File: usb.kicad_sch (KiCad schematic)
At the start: 14 parts, among them J201 GT-USB-7010ASV, Q201 S8050, Q202 S8050, U202 CP2104

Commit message: Update to kicad 9
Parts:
- J201: value GT-USB-7010ASV -> GT-USB-7010ASV

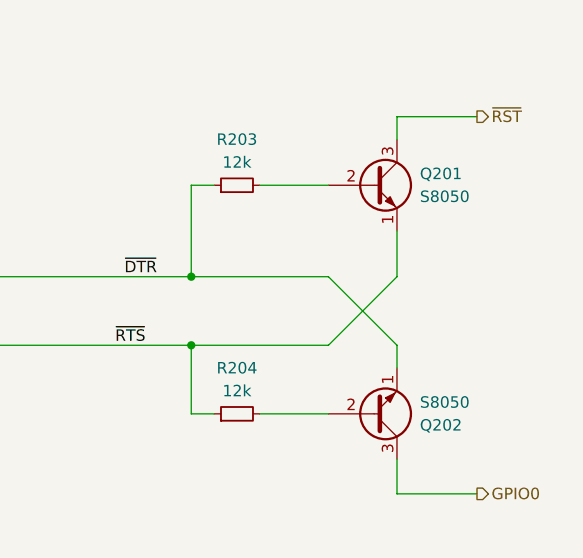
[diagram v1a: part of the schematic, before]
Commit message: Fix hardware flow control transistor pinouts
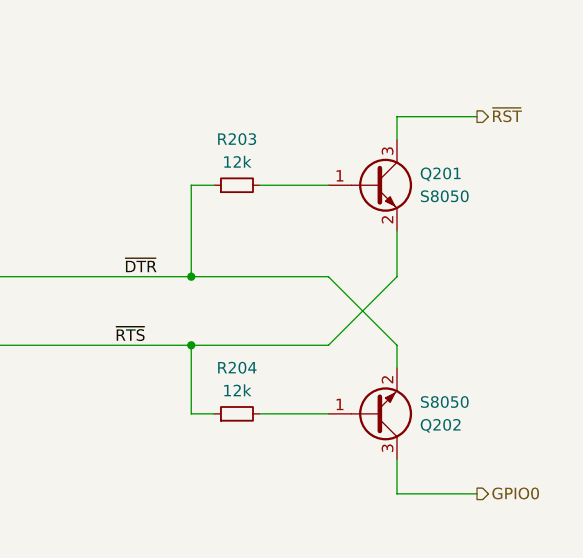
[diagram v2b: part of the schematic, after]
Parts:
- Q201, Q202: symbol Transistor_BJT:S8050 -> Transistor_BJT:Q_NPN_BEC
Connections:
- net ~{DTR}: now also Q202.2 (E); no longer Q202.1 (E)
- net ~{RTS}: now also Q201.2 (E); no longer Q201.1 (E)
- net at R204.2: now also Q202.1 (B); no longer Q202.2 (B)
- net at R203.2: now also Q201.1 (B); no longer Q201.2 (B)
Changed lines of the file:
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@@
 	)
 	(symbol
-		(lib_id "Transistor_BJT:S8050")
+		(lib_id "Transistor_BJT:Q_NPN_BEC")
 		(at 256.54 119.38 0)
 		(mirror x)
@@
 		)
 		(property "Footprint" "Package_TO_SOT_SMD:SOT-23-3"
-			(at 261.62 117.475 0)
-			(effects
-				(font
-					(size 1.27 1.27)
-					(italic yes)
-				)
-				(justify left)
-				(hide yes)
-			)
-		)
-		(property "Datasheet" "http://www.unisonic.com.tw/datasheet/S8050.pdf"
+			(at 261.62 121.92 0)
+			(effects
+				(font
+					(size 1.27 1.27)
+				)
+				(hide yes)
+			)
+		)
+		(property "Datasheet" "https://www.lcsc.com/datasheet/C2891804.pdf"
 			(at 256.54 119.38 0)
 			(effects
@@
 					(size 1.27 1.27)
 				)
-				(justify left)
-				(hide yes)
-			)
-		)
-		(property "Description" "0.7A Ic, 20V Vce, Low Voltage High Current NPN Transistor, TO-92"
+				(hide yes)
+			)
+		)
+		(property "Description" "Bipolar (BJT) Transistor NPN 25 V 500 mA 150MHz 300 mW Surface Mount SOT-23"
 			(at 256.54 119.38 0)
 			(effects
@@
 	)
 	(symbol
-		(lib_id "Transistor_BJT:S8050")
+		(lib_id "Transistor_BJT:Q_NPN_BEC")
 		(at 256.54 93.98 0)
 		(unit 1)
@@
 		(fields_autoplaced yes)
 		(property "Reference" "Q201"
-			(at 261.62 92.71 0)
+			(at 261.62 92.7099 0)
 			(effects
 				(font
@@
 		)
 		(property "Value" "S8050"
-			(at 261.62 95.25 0)
+			(at 261.62 95.2499 0)
 			(effects
 				(font
@@
 		)
 		(property "Footprint" "Package_TO_SOT_SMD:SOT-23-3"
-			(at 261.62 95.885 0)
-			(effects
-				(font
-					(size 1.27 1.27)
-					(italic yes)
-				)
-				(justify left)
-				(hide yes)
-			)
-		)
-		(property "Datasheet" "http://www.unisonic.com.tw/datasheet/S8050.pdf"
+			(at 261.62 91.44 0)
+			(effects
+				(font
+					(size 1.27 1.27)
+				)
+				(hide yes)
+			)
+		)
+		(property "Datasheet" "https://www.lcsc.com/datasheet/C2891804.pdf"
 			(at 256.54 93.98 0)
 			(effects
@@
 					(size 1.27 1.27)
 				)
-				(justify left)
-				(hide yes)
-			)
-		)
-		(property "Description" "0.7A Ic, 20V Vce, Low Voltage High Current NPN Transistor, TO-92"
+				(hide yes)
+			)
+		)
+		(property "Description" "Bipolar (BJT) Transistor NPN 25 V 500 mA 150MHz 300 mW Surface Mount SOT-23"
 			(at 256.54 93.98 0)
 			(effects

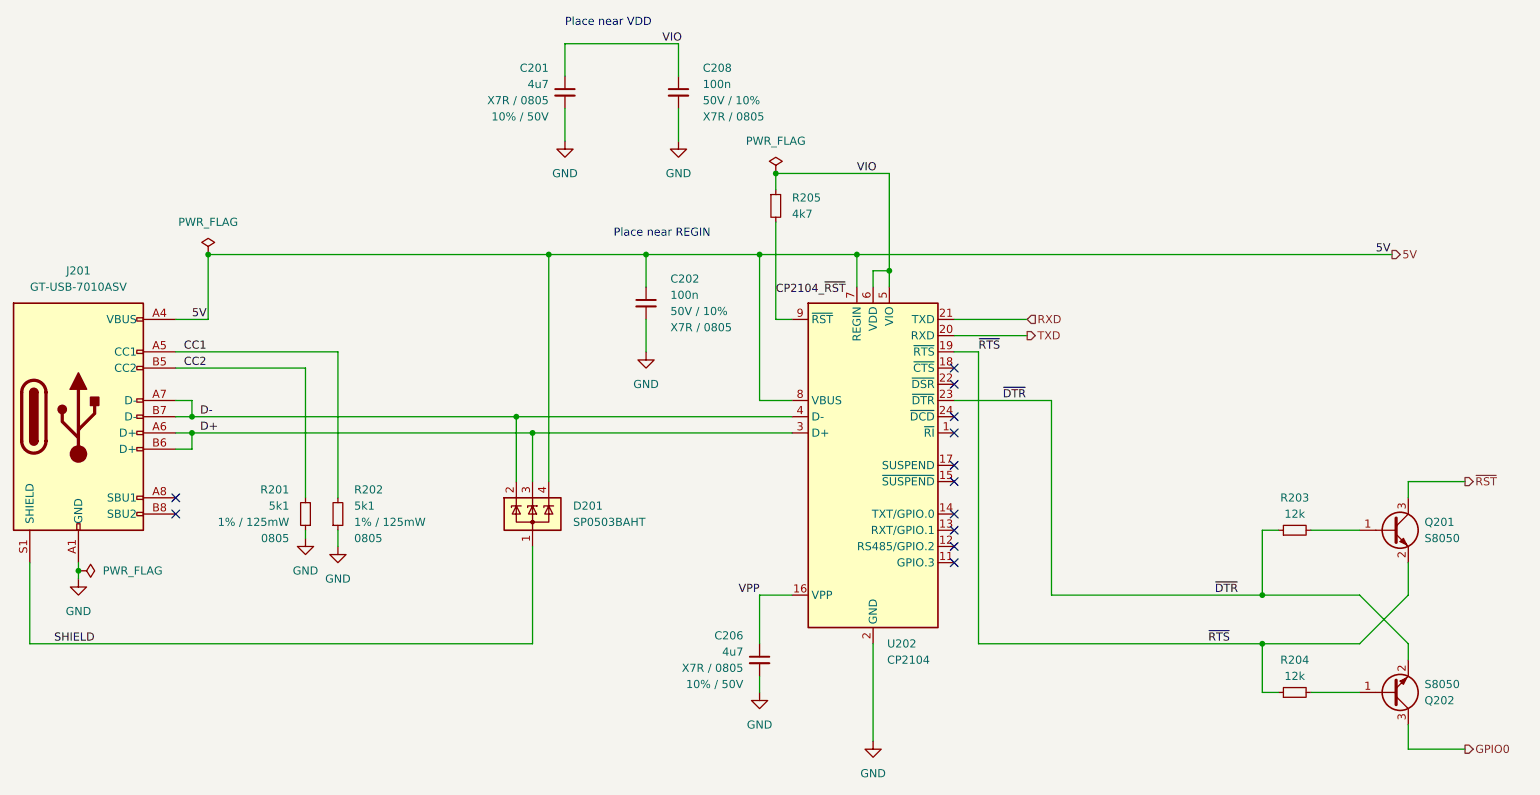
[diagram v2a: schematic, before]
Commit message: Update reference designators to single digit
Fits on the silk better
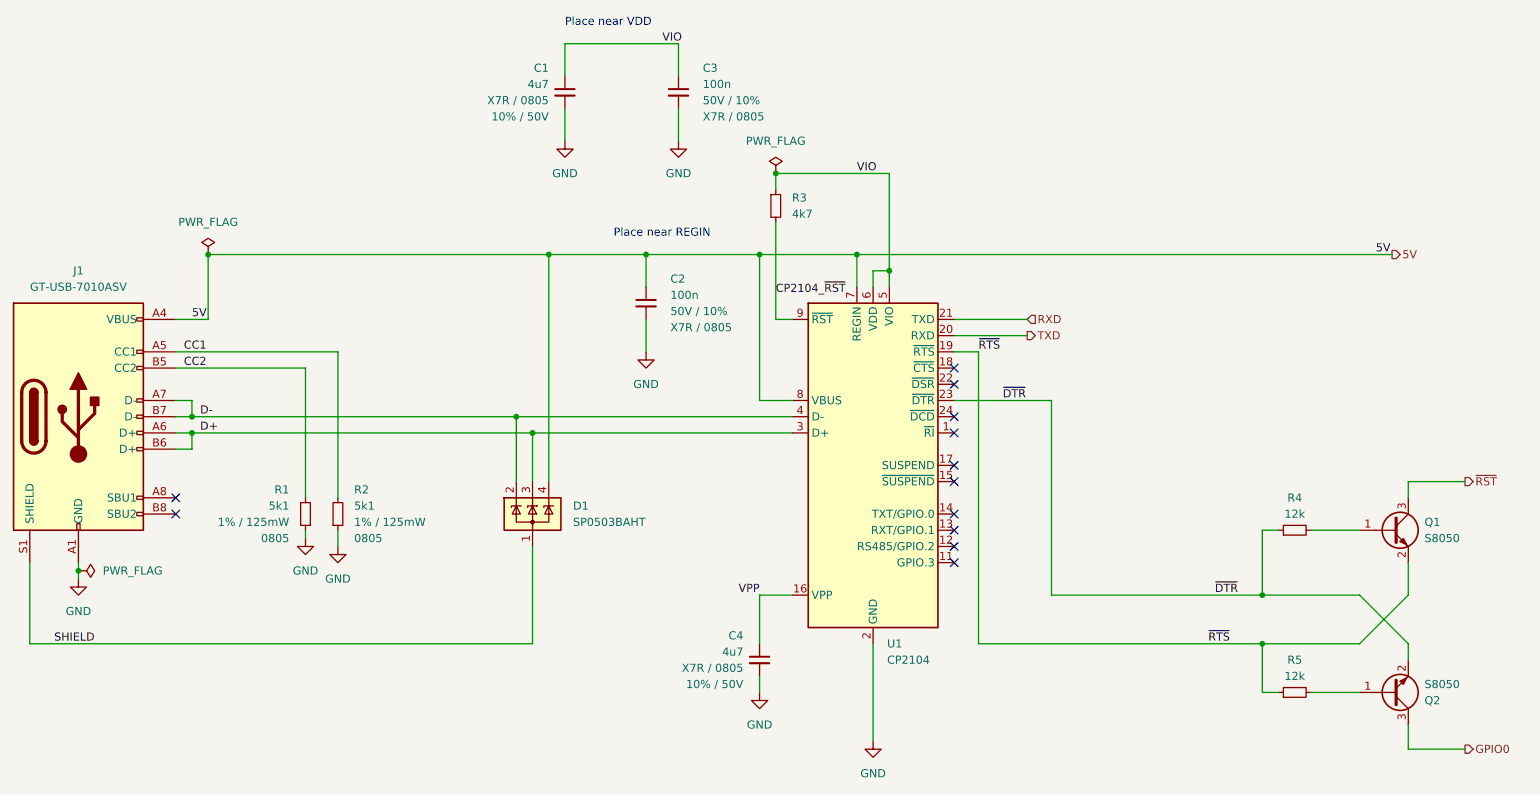
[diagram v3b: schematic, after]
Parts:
- renumbered C201 to C1, C202 to C2, C208 to C3, C206 to C4, D201 to D1, J201 to J1, Q201 to Q1, Q202 to Q2, R201 to R1, R202 to R2, R205 to R3, R203 to R4, R204 to R5, U202 to U1
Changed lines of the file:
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@@
 		(dnp no)
 		(fields_autoplaced yes)
-		(property "Reference" "#FLG03"
+		(property "Reference" "#FLG01"
 			(at 52.705 100.33 0)
 			(effects
@@
 			(project "youdbetterrun"
 				(path "/50da2b4e-34b1-4787-8ee6-5d7d17f804f4/951b5697-f1e3-4d2e-841e-7032f41eb35f"
-					(reference "#FLG03")
+					(reference "#FLG01")
 					(unit 1)
 				)
@@
 		(dnp no)
 		(fields_autoplaced yes)
-		(property "Reference" "J201"
+		(property "Reference" "J1"
 			(at 50.8 53.34 0)
 			(effects
@@
 			(project "youdbetterrun"
 				(path "/50da2b4e-34b1-4787-8ee6-5d7d17f804f4/951b5697-f1e3-4d2e-841e-7032f41eb35f"
-					(reference "J201")
+					(reference "J1")
 					(unit 1)
 				)
@@
 		(on_board yes)
 		(dnp no)
-		(property "Reference" "Q202"
+		(property "Reference" "Q2"
 			(at 261.62 120.65 0)
 			(effects
@@
 			(project "youdbetterrun"
 				(path "/50da2b4e-34b1-4787-8ee6-5d7d17f804f4/951b5697-f1e3-4d2e-841e-7032f41eb35f"
-					(reference "Q202")
+					(reference "Q2")
 					(unit 1)
 				)
@@
 		(on_board yes)
 		(dnp no)
-		(property "Reference" "R202"
+		(property "Reference" "R2"
 			(at 93.98 87.63 0)
 			(effects
@@
 			(project "youdbetterrun"
 				(path "/50da2b4e-34b1-4787-8ee6-5d7d17f804f4/951b5697-f1e3-4d2e-841e-7032f41eb35f"
-					(reference "R202")
+					(reference "R2")
 					(unit 1)
 				)
@@
 		(dnp no)
 		(fields_autoplaced yes)
-		(property "Reference" "#FLG02"
+		(property "Reference" "#FLG03"
 			(at 160.02 36.195 0)
 			(effects
@@
 			(project "youdbetterrun"
 				(path "/50da2b4e-34b1-4787-8ee6-5d7d17f804f4/951b5697-f1e3-4d2e-841e-7032f41eb35f"
-					(reference "#FLG02")
+					(reference "#FLG03")
 					(unit 1)
 				)
@@
 		(dnp no)
 		(fields_autoplaced yes)
-		(property "Reference" "#PWR0206"
+		(property "Reference" "#PWR08"
 			(at 175.26 133.35 0)
 			(effects
@@
 			(project "youdbetterrun"
 				(path "/50da2b4e-34b1-4787-8ee6-5d7d17f804f4/951b5697-f1e3-4d2e-841e-7032f41eb35f"
-					(reference "#PWR0206")
+					(reference "#PWR08")
 					(unit 1)
 				)
@@
 		(dnp no)
 		(fields_autoplaced yes)
-		(property "Reference" "#PWR0207"
+		(property "Reference" "#PWR01"
 			(at 50.8 107.95 0)
 			(effects
@@
 			(project "youdbetterrun"
 				(path "/50da2b4e-34b1-4787-8ee6-5d7d17f804f4/951b5697-f1e3-4d2e-841e-7032f41eb35f"
-					(reference "#PWR0207")
+					(reference "#PWR01")
 					(unit 1)
 				)
@@
 		(on_board yes)
 		(dnp no)
-		(property "Reference" "C208"
+		(property "Reference" "C3"
 			(at 148.59 21.59 0)
 			(effects
@@
 			(project "youdbetterrun"
 				(path "/50da2b4e-34b1-4787-8ee6-5d7d17f804f4/951b5697-f1e3-4d2e-841e-7032f41eb35f"
-					(reference "C208")
+					(reference "C3")
 					(unit 1)
 				)
@@
 		(dnp no)
 		(fields_autoplaced yes)
-		(property "Reference" "#PWR0213"
+		(property "Reference" "#PWR06"
 			(at 144.78 39.37 0)
 			(effects
@@
 			(project "youdbetterrun"
 				(path "/50da2b4e-34b1-4787-8ee6-5d7d17f804f4/951b5697-f1e3-4d2e-841e-7032f41eb35f"
-					(reference "#PWR0213")
+					(reference "#PWR06")
 					(unit 1)
 				)
@@
 		(dnp no)
 		(fields_autoplaced yes)
-		(property "Reference" "R205"
+		(property "Reference" "R3"
 			(at 162.56 41.91 0)
 			(effects
@@
 			(project "youdbetterrun"
 				(path "/50da2b4e-34b1-4787-8ee6-5d7d17f804f4/951b5697-f1e3-4d2e-841e-7032f41eb35f"
-					(reference "R205")
+					(reference "R3")
 					(unit 1)
 				)
@@
 		(on_board yes)
 		(dnp no)
-		(property "Reference" "R203"
+		(property "Reference" "R4"
 			(at 241.3 88.9 90)
 			(effects
@@
 			(project "youdbetterrun"
 				(path "/50da2b4e-34b1-4787-8ee6-5d7d17f804f4/951b5697-f1e3-4d2e-841e-7032f41eb35f"
-					(reference "R203")
+					(reference "R4")
 					(unit 1)
 				)
@@
 		(dnp no)
 		(fields_autoplaced yes)
-		(property "Reference" "#PWR0212"
+		(property "Reference" "#PWR07"
 			(at 157.48 125.73 0)
 			(effects
@@
 			(project "youdbetterrun"
 				(path "/50da2b4e-34b1-4787-8ee6-5d7d17f804f4/951b5697-f1e3-4d2e-841e-7032f41eb35f"
-					(reference "#PWR0212")
+					(reference "#PWR07")
 					(unit 1)
 				)
@@
 		(on_board yes)
 		(dnp no)
-		(property "Reference" "C206"
+		(property "Reference" "C4"
 			(at 154.94 110.49 0)
 			(effects
@@
 			(project "youdbetterrun"
 				(path "/50da2b4e-34b1-4787-8ee6-5d7d17f804f4/951b5697-f1e3-4d2e-841e-7032f41eb35f"
-					(reference "C206")
+					(reference "C4")
 					(unit 1)
 				)
@@
 		(on_board yes)
 		(dnp no)
-		(property "Reference" "C201"
+		(property "Reference" "C1"
 			(at 124.46 21.59 0)
 			(effects
@@
 			(project "youdbetterrun"
 				(path "/50da2b4e-34b1-4787-8ee6-5d7d17f804f4/951b5697-f1e3-4d2e-841e-7032f41eb35f"
-					(reference "C201")
+					(reference "C1")
 					(unit 1)
 				)
@@
 		(dnp no)
 		(fields_autoplaced yes)
-		(property "Reference" "U202"
+		(property "Reference" "U1"
 			(at 177.4541 111.76 0)
 			(effects
@@
 			(project "youdbetterrun"
 				(path "/50da2b4e-34b1-4787-8ee6-5d7d17f804f4/951b5697-f1e3-4d2e-841e-7032f41eb35f"
-					(reference "U202")
+					(reference "U1")
 					(unit 1)
 				)
@@
 		(on_board yes)
 		(dnp no)
-		(property "Reference" "R204"
+		(property "Reference" "R5"
 			(at 241.3 114.3 90)
 			(effects
@@
 			(project "youdbetterrun"
 				(path "/50da2b4e-34b1-4787-8ee6-5d7d17f804f4/951b5697-f1e3-4d2e-841e-7032f41eb35f"
-					(reference "R204")
+					(reference "R5")
 					(unit 1)
 				)
@@
 		(dnp no)
 		(fields_autoplaced yes)
-		(property "Reference" "D201"
+		(property "Reference" "D1"
 			(at 128.27 90.17 0)
 			(effects
@@
 			(project "youdbetterrun"
 				(path "/50da2b4e-34b1-4787-8ee6-5d7d17f804f4/951b5697-f1e3-4d2e-841e-7032f41eb35f"
-					(reference "D201")
+					(reference "D1")
 					(unit 1)
 				)
@@
 		(on_board yes)
 		(dnp no)
-		(property "Reference" "R201"
+		(property "Reference" "R1"
 			(at 83.82 87.63 0)
 			(effects
@@
 			(project "youdbetterrun"
 				(path "/50da2b4e-34b1-4787-8ee6-5d7d17f804f4/951b5697-f1e3-4d2e-841e-7032f41eb35f"
-					(reference "R201")
+					(reference "R1")
 					(unit 1)
 				)
@@
 		(dnp no)
 		(fields_autoplaced yes)
-		(property "Reference" "#FLG01"
+		(property "Reference" "#FLG02"
 			(at 71.12 48.895 0)
 			(effects
@@
 			(project "youdbetterrun"
 				(path "/50da2b4e-34b1-4787-8ee6-5d7d17f804f4/951b5697-f1e3-4d2e-841e-7032f41eb35f"
-					(reference "#FLG01")
+					(reference "#FLG02")
 					(unit 1)
 				)
@@
 		(dnp no)
 		(fields_autoplaced yes)
-		(property "Reference" "#PWR0202"
+		(property "Reference" "#PWR05"
 			(at 139.7 72.39 0)
 			(effects
@@
 			(project "youdbetterrun"
 				(path "/50da2b4e-34b1-4787-8ee6-5d7d17f804f4/951b5697-f1e3-4d2e-841e-7032f41eb35f"
-					(reference "#PWR0202")
+					(reference "#PWR05")
 					(unit 1)
 				)
@@
 		(on_board yes)
 		(dnp no)
-		(property "Reference" "C202"
+		(property "Reference" "C2"
 			(at 143.51 54.61 0)
 			(effects
@@
 			(project "youdbetterrun"
 				(path "/50da2b4e-34b1-4787-8ee6-5d7d17f804f4/951b5697-f1e3-4d2e-841e-7032f41eb35f"
-					(reference "C202")
+					(reference "C2")
 					(unit 1)
 				)
@@
 		(dnp no)
 		(fields_autoplaced yes)
-		(property "Reference" "#PWR0205"
+		(property "Reference" "#PWR03"
 			(at 91.44 102.87 0)
 			(effects
@@
 			(project "youdbetterrun"
 				(path "/50da2b4e-34b1-4787-8ee6-5d7d17f804f4/951b5697-f1e3-4d2e-841e-7032f41eb35f"
-					(reference "#PWR0205")
+					(reference "#PWR03")
 					(unit 1)
 				)
@@
 		(dnp no)
 		(fields_autoplaced yes)
-		(property "Reference" "Q201"
+		(property "Reference" "Q1"
 			(at 261.62 92.7099 0)
 			(effects
@@
 			(project "youdbetterrun"
 				(path "/50da2b4e-34b1-4787-8ee6-5d7d17f804f4/951b5697-f1e3-4d2e-841e-7032f41eb35f"
-					(reference "Q201")
+					(reference "Q1")
 					(unit 1)
 				)
@@
 		(dnp no)
 		(fields_autoplaced yes)
-		(property "Reference" "#PWR0201"
+		(property "Reference" "#PWR04"
 			(at 127 39.37 0)
 			(effects
@@
 			(project "youdbetterrun"
 				(path "/50da2b4e-34b1-4787-8ee6-5d7d17f804f4/951b5697-f1e3-4d2e-841e-7032f41eb35f"
-					(reference "#PWR0201")
+					(reference "#PWR04")
 					(unit 1)
 				)
@@
 		(dnp no)
 		(fields_autoplaced yes)
-		(property "Reference" "#PWR0204"
+		(property "Reference" "#PWR02"
 			(at 86.36 101.6 0)
 			(effects
@@
 			(project "youdbetterrun"
 				(path "/50da2b4e-34b1-4787-8ee6-5d7d17f804f4/951b5697-f1e3-4d2e-841e-7032f41eb35f"
-					(reference "#PWR0204")
-					(unit 1)
-				)
+					(reference "#PWR02")
+					(unit 1)
+				)
